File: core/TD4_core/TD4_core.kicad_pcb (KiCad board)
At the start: 2 copper layers, 190 x 160 mm, 98 parts, among them J1 Conn_02x32_Row_Letter_First, J2 Conn_01x04, J3 Conn_01x04, J4 Conn_01x04, U1 74HC161, U10 74LS151, U11 74AHC1G04, U12 74AHC1G04, U13 74AHC1G86, U14 74AHC1G04, U15 74AHC1G86, U16 74HC86, U17 74HC04, U18 74HC21, U19 74HC86, U2 74HC161, U20 74HC04, U21 74HC86, U22 74HC04, U23 74HC86, U24 74HC04, U25 74HC21, U26 74HC86, U27 74HC04, U28 74HC21, U29 74HC153, U3 74HC161, U30 74HC153, U31 74HC74, U32 74HC175, U33 74AHC1G08, U34 74HC125, U35 74HC175, U36 74AHC1G08, U37 74HC155, U38 74HC125, U39 74HC125, U4 74HC161, U40 74HC125, U5 74HC86, U6 74HC08, U7 74HC32, U8 74HC86, U9 74HC08

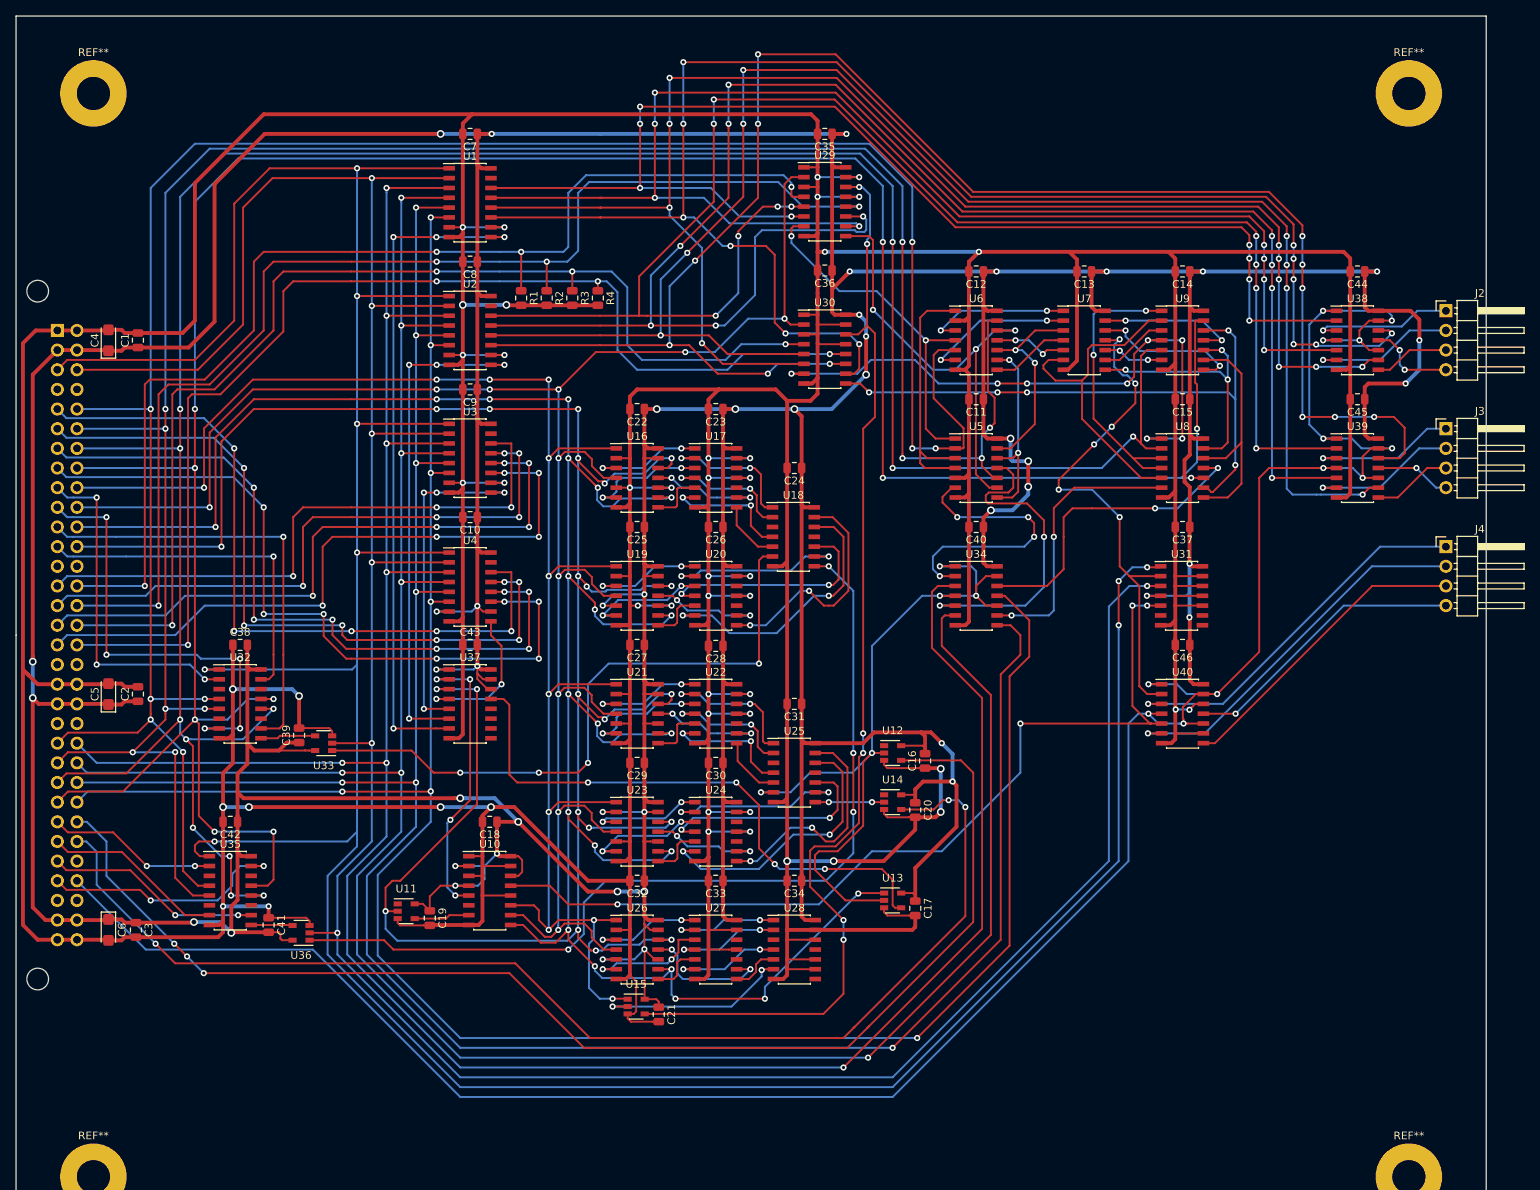
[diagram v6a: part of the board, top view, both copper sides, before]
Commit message: Replaced debug headers with vertical ones
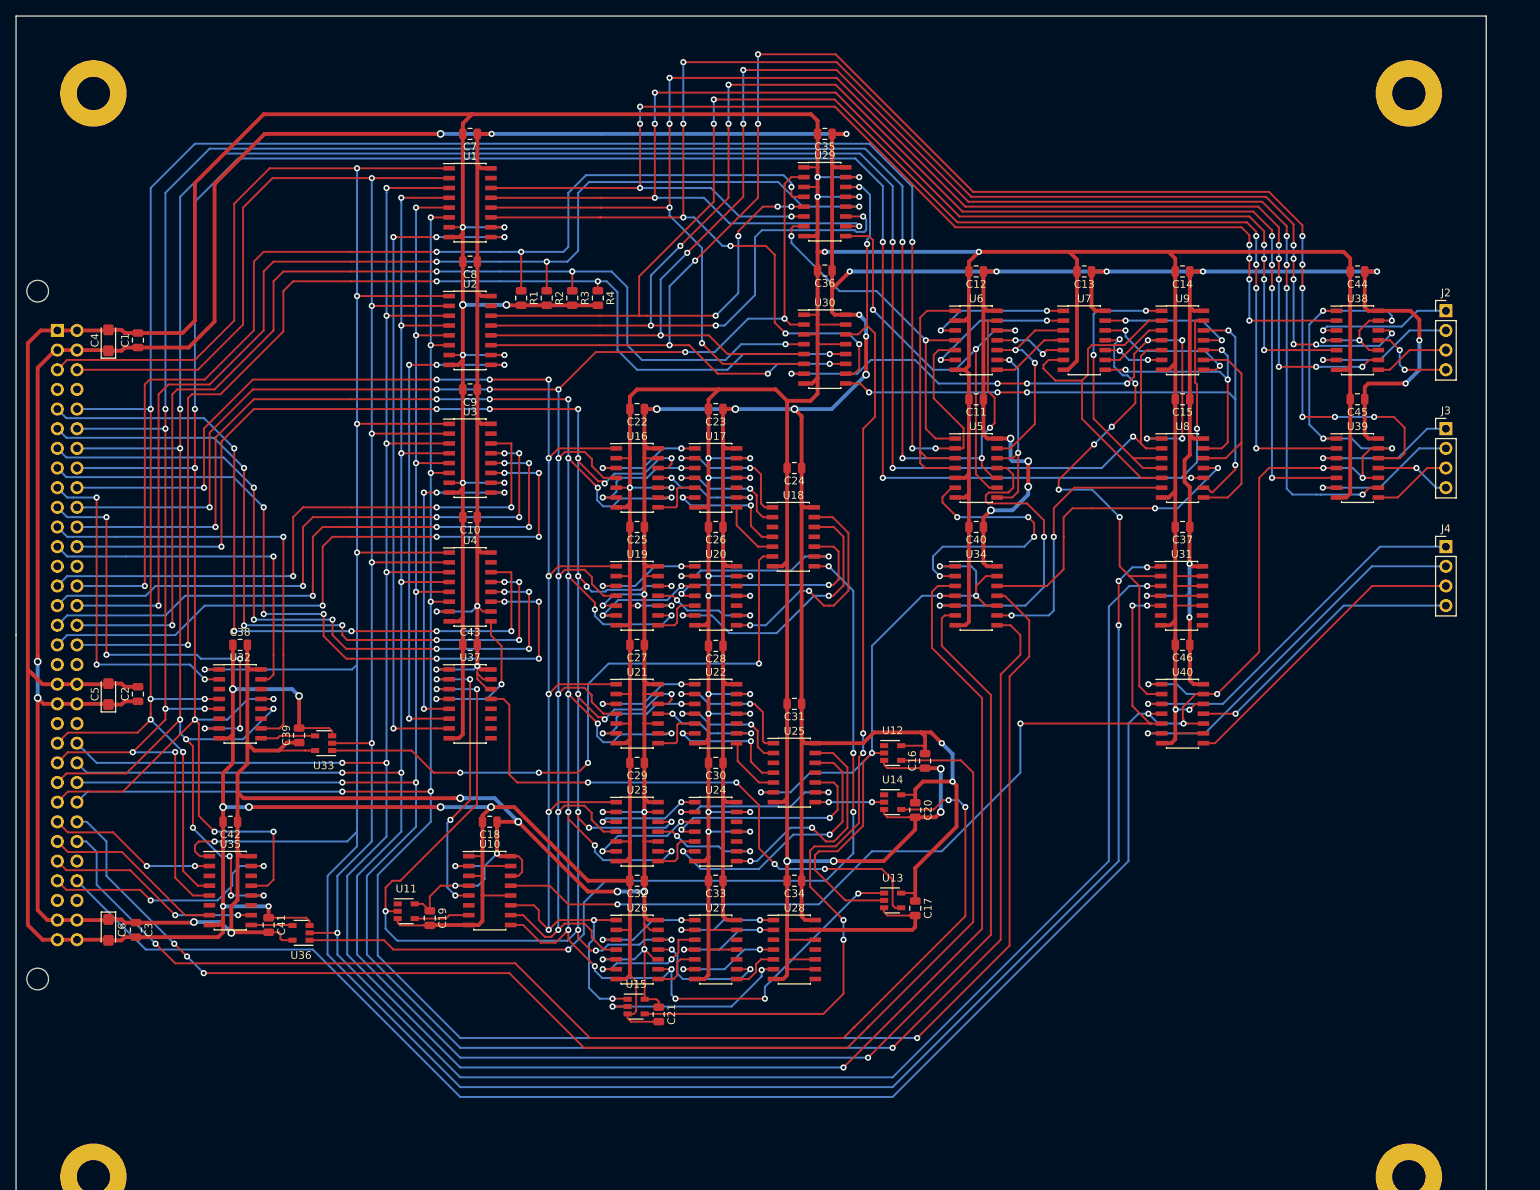
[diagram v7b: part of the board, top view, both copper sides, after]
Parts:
- J2, J3, J4: footprint Connector_PinHeader_2.54mm:PinHeader_1x04_P2.54mm_Horizontal -> Connector_PinHeader_2.54mm:PinHeader_1x04_P2.54mm_Vertical
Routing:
- net GND: track 1340.2 -> 1338.3 mm
- net VCC: track 1147.2 -> 1146.7 mm

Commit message: Minor changes to PCB
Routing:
- net /C_r: track 118.5 -> 114.8 mm
- net /4-bit 3-state buffer/A3: track 40.7 -> 39.3 mm
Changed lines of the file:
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@@
     (thickness 1.6)
     (drawings 5)
-    (tracks 3149)
+    (tracks 3150)
     (zones 0)
     (modules 98)
@@
   (via (at 195.707 72.644) (size 0.8) (drill 0.4) (layers F.Cu B.Cu) (net 102))
   (segment (start 193.835 72.644) (end 195.707 72.644) (width 0.25) (layer F.Cu) (net 102))
-  (segment (start 187.579 77.851) (end 179.451 77.851) (width 0.25) (layer F.Cu) (net 102))
-  (segment (start 175.768 81.534) (end 175.768 78.994) (width 0.25) (layer F.Cu) (net 102))
+  (segment (start 179.451 77.851) (end 187.579 77.851) (width 0.25) (layer F.Cu) (net 102))
   (segment (start 176.911 77.851) (end 179.451 77.851) (width 0.25) (layer F.Cu) (net 102))
+  (segment (start 167.165 87.884) (end 171.196 87.884) (width 0.25) (layer F.Cu) (net 102))
+  (segment (start 171.196 87.884) (end 175.768 83.312) (width 0.25) (layer F.Cu) (net 102))
+  (segment (start 175.768 83.312) (end 175.768 78.994) (width 0.25) (layer F.Cu) (net 102))
   (segment (start 175.768 78.994) (end 176.911 77.851) (width 0.25) (layer F.Cu) (net 102))
-  (segment (start 167.165 87.884) (end 173.609 87.884) (width 0.25) (layer F.Cu) (net 102))
-  (segment (start 175.768 85.725) (end 175.768 81.534) (width 0.25) (layer F.Cu) (net 102))
-  (segment (start 173.609 87.884) (end 175.768 85.725) (width 0.25) (layer F.Cu) (net 102))
   (via (at 184.658 90.424) (size 0.8) (drill 0.4) (layers F.Cu B.Cu) (net 103))
   (segment (start 184.658 103.402002) (end 184.658 90.424) (width 0.25) (layer F.Cu) (net 103))
@@
   (segment (start 111.76 129.032) (end 118.11 129.032) (width 0.25) (layer F.Cu) (net 103))
   (segment (start 109.347 126.619) (end 111.76 129.032) (width 0.25) (layer F.Cu) (net 103))
-  (segment (start 118.11 129.032) (end 144.145 129.032) (width 0.25) (layer B.Cu) (net 103))
-  (segment (start 144.145 129.032) (end 151.003 122.174) (width 0.25) (layer B.Cu) (net 103))
-  (segment (start 151.003 122.174) (end 160.02 122.174) (width 0.25) (layer B.Cu) (net 103))
-  (segment (start 170.18 112.014) (end 170.18 105.664) (width 0.25) (layer B.Cu) (net 103))
-  (via (at 170.18 105.664) (size 0.8) (drill 0.4) (layers F.Cu B.Cu) (net 103))
-  (segment (start 160.02 122.174) (end 170.18 112.014) (width 0.25) (layer B.Cu) (net 103))
-  (segment (start 170.18 105.664) (end 187.071 105.664) (width 0.25) (layer F.Cu) (net 103))
   (segment (start 187.071 105.664) (end 186.919998 105.664) (width 0.25) (layer F.Cu) (net 103))
   (segment (start 188.435 105.664) (end 187.071 105.664) (width 0.25) (layer F.Cu) (net 103))
+  (via (at 177.927 105.663992) (size 0.8) (drill 0.4) (layers F.Cu B.Cu) (net 103))
+  (segment (start 187.070992 105.663992) (end 178.492685 105.663992) (width 0.25) (layer F.Cu) (net 103))
+  (segment (start 187.071 105.664) (end 187.070992 105.663992) (width 0.25) (layer F.Cu) (net 103))
+  (segment (start 178.492685 105.663992) (end 177.927 105.663992) (width 0.25) (layer F.Cu) (net 103))
+  (segment (start 177.527001 106.063991) (end 177.927 105.663992) (width 0.25) (layer B.Cu) (net 103))
+  (segment (start 144.145 129.032) (end 151.257 121.92) (width 0.25) (layer B.Cu) (net 103))
+  (segment (start 151.257 121.92) (end 161.670992 121.92) (width 0.25) (layer B.Cu) (net 103))
+  (segment (start 118.11 129.032) (end 144.145 129.032) (width 0.25) (layer B.Cu) (net 103))
+  (segment (start 161.670992 121.92) (end 177.527001 106.063991) (width 0.25) (layer B.Cu) (net 103))
   (segment (start 91.905 130.871) (end 95.951 130.871) (width 0.25) (layer F.Cu) (net 104))
   (segment (start 96.393 130.429) (end 98.9 130.429) (width 0.25) (layer F.Cu) (net 104))
